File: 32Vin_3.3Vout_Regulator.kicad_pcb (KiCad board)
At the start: 2 copper layers, 11.4 x 18.3 mm, 9 parts, among them J1 PinSocket_1x04_P2.54mm_Vertic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, U1 AP63203WU

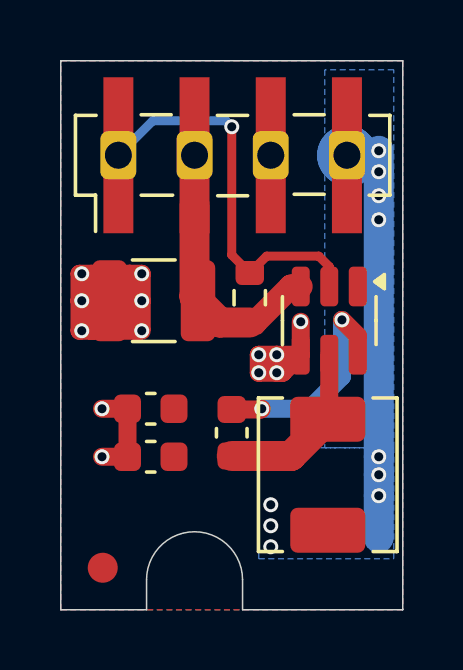
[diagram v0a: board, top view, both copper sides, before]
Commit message: Reduce screw hole size to match M2
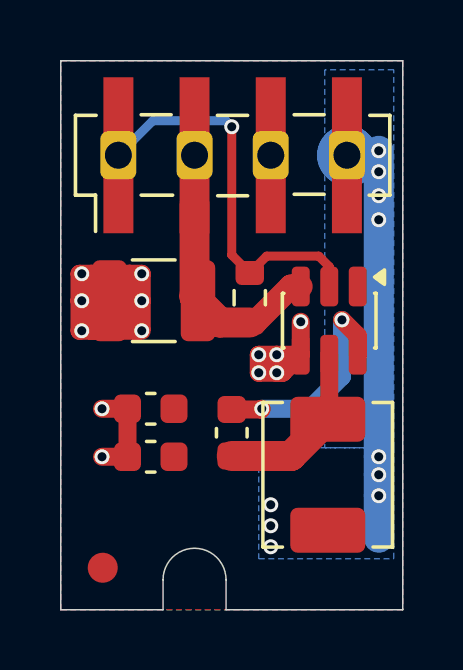
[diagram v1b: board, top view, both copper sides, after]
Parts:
- J1: value PinSocket_1x04_P2.54mm_Vertical_SMD_Pin1Left -> Regulator
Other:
- outline, holes or cut-outs redrawn
